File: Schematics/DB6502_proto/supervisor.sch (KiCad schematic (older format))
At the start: 32 parts, among them J9 Clock divider, SW1 Reset, U10 FT230XS, U11 74HC595, U12 74HC157, U13 ATmega644PA-PU, U14 74AC74, U15 DS1813, U16 74AC74, U17 74AC08, U8 74AC04, X1 8MHz, Y1 20MHz

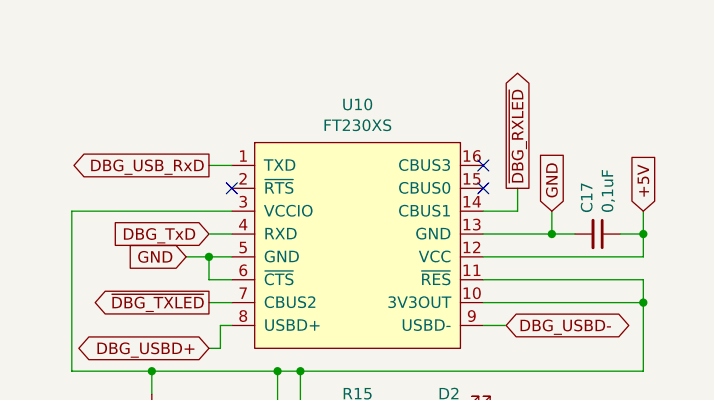
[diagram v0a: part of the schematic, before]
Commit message: Most chips placed, tracing continues
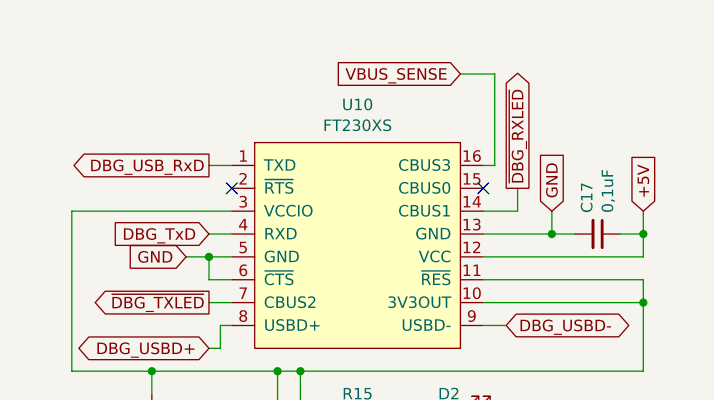
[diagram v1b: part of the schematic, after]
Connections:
- net VBUS_SENSE: now reaches U10.16 (CBUS3)
- no-connect marks 14 -> 13
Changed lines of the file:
@@
 	10300 1250 10450 1250
 NoConn ~ 10300 1150
-NoConn ~ 10300 1050
 $Comp
 L 74xx:74HC595 U11
@@
 	1    0    0    -1
 $EndComp
+Text GLabel 10200 650  0    50   Input ~ 0
+VBUS_SENSE
+Wire Wire Line
+	10300 1050 10350 1050
+Wire Wire Line
+	10350 1050 10350 650
+Wire Wire Line
+	10350 650  10200 650
 Wire Bus Line
 	3200 2200 3200 2900

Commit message: Increased capacitor footprints to 1206
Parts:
- C14, C15, C16, C17, C20, C21, C22, C23, C24, C25, C26: footprint Capacitor_SMD:C_0805_2012Metric_Pad1.15x1.40mm_HandSolder -> Capacitor_SMD:C_1206_3216Metric_Pad1.42x1.75mm_HandSolder
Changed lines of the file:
@@
 F 0 "C20" V 1350 1800 50  0000 C CNN
 F 1 "0,1uF" V 1250 1800 50  0000 C CNN
-F 2 "Capacitor_SMD:C_0805_2012Metric_Pad1.15x1.40mm_HandSolder" H 1500 1800 50  0001 C CNN
+F 2 "Capacitor_SMD:C_1206_3216Metric_Pad1.42x1.75mm_HandSolder" H 1500 1800 50  0001 C CNN
 F 3 "~" H 1500 1800 50  0001 C CNN
 	1    1500 1800
@@
 F 0 "C23" H 1342 6746 50  0000 L CNN
 F 1 "0,1uF" H 1342 6655 50  0000 L CNN
-F 2 "Capacitor_SMD:C_0805_2012Metric_Pad1.15x1.40mm_HandSolder" H 1250 6700 50  0001 C CNN
+F 2 "Capacitor_SMD:C_1206_3216Metric_Pad1.42x1.75mm_HandSolder" H 1250 6700 50  0001 C CNN
 F 3 "~" H 1250 6700 50  0001 C CNN
 	1    1250 6700
@@
 F 0 "C24" H 2292 6746 50  0000 L CNN
 F 1 "0,1uF" H 2292 6655 50  0000 L CNN
-F 2 "Capacitor_SMD:C_0805_2012Metric_Pad1.15x1.40mm_HandSolder" H 2200 6700 50  0001 C CNN
+F 2 "Capacitor_SMD:C_1206_3216Metric_Pad1.42x1.75mm_HandSolder" H 2200 6700 50  0001 C CNN
 F 3 "~" H 2200 6700 50  0001 C CNN
 	1    2200 6700
@@
 F 0 "C15" V 6921 800 50  0000 C CNN
 F 1 "0,1uF" V 7012 800 50  0000 C CNN
-F 2 "Capacitor_SMD:C_0805_2012Metric_Pad1.15x1.40mm_HandSolder" H 7150 800 50  0001 C CNN
+F 2 "Capacitor_SMD:C_1206_3216Metric_Pad1.42x1.75mm_HandSolder" H 7150 800 50  0001 C CNN
 F 3 "~" H 7150 800 50  0001 C CNN
 	1    7150 800
@@
 F 0 "C14" V 1871 800 50  0000 C CNN
 F 1 "0,1uF" V 1962 800 50  0000 C CNN
-F 2 "Capacitor_SMD:C_0805_2012Metric_Pad1.15x1.40mm_HandSolder" H 2100 800 50  0001 C CNN
+F 2 "Capacitor_SMD:C_1206_3216Metric_Pad1.42x1.75mm_HandSolder" H 2100 800 50  0001 C CNN
 F 3 "~" H 2100 800 50  0001 C CNN
 	1    2100 800
@@
 F 0 "C16" V 4721 900 50  0000 C CNN
 F 1 "0,1uF" V 4812 900 50  0000 C CNN
-F 2 "Capacitor_SMD:C_0805_2012Metric_Pad1.15x1.40mm_HandSolder" H 4950 900 50  0001 C CNN
+F 2 "Capacitor_SMD:C_1206_3216Metric_Pad1.42x1.75mm_HandSolder" H 4950 900 50  0001 C CNN
 F 3 "~" H 4950 900 50  0001 C CNN
 	1    4950 900
@@
 F 0 "C17" H 10708 1304 50  0000 R CNN
 F 1 "0,1uF" H 10708 1395 50  0000 R CNN
-F 2 "Capacitor_SMD:C_0805_2012Metric_Pad1.15x1.40mm_HandSolder" H 10800 1350 50  0001 C CNN
+F 2 "Capacitor_SMD:C_1206_3216Metric_Pad1.42x1.75mm_HandSolder" H 10800 1350 50  0001 C CNN
 F 3 "~" H 10800 1350 50  0001 C CNN
 	1    10800 1350
@@
 F 0 "C21" H 8965 2196 50  0000 L CNN
 F 1 "0,1uF" H 8965 2105 50  0000 L CNN
-F 2 "Capacitor_SMD:C_0805_2012Metric_Pad1.15x1.40mm_HandSolder" H 8888 2000 50  0001 C CNN
+F 2 "Capacitor_SMD:C_1206_3216Metric_Pad1.42x1.75mm_HandSolder" H 8888 2000 50  0001 C CNN
 F 3 "~" H 8850 2150 50  0001 C CNN
 	1    8850 2150
@@
 F 0 "C22" H 4600 4000 50  0000 R CNN
 F 1 "0,1uF" H 4600 3900 50  0000 R CNN
-F 2 "Capacitor_SMD:C_0805_2012Metric_Pad1.15x1.40mm_HandSolder" H 4700 3950 50  0001 C CNN
+F 2 "Capacitor_SMD:C_1206_3216Metric_Pad1.42x1.75mm_HandSolder" H 4700 3950 50  0001 C CNN
 F 3 "~" H 4700 3950 50  0001 C CNN
 	1    4700 3950
@@
 F 0 "C25" H 3242 6746 50  0000 L CNN
 F 1 "0,1uF" H 3242 6655 50  0000 L CNN
-F 2 "Capacitor_SMD:C_0805_2012Metric_Pad1.15x1.40mm_HandSolder" H 3150 6700 50  0001 C CNN
+F 2 "Capacitor_SMD:C_1206_3216Metric_Pad1.42x1.75mm_HandSolder" H 3150 6700 50  0001 C CNN
 F 3 "~" H 3150 6700 50  0001 C CNN
 	1    3150 6700
@@
 F 0 "C26" H 4242 6746 50  0000 L CNN
 F 1 "0,1uF" H 4242 6655 50  0000 L CNN
-F 2 "Capacitor_SMD:C_0805_2012Metric_Pad1.15x1.40mm_HandSolder" H 4150 6700 50  0001 C CNN
+F 2 "Capacitor_SMD:C_1206_3216Metric_Pad1.42x1.75mm_HandSolder" H 4150 6700 50  0001 C CNN
 F 3 "~" H 4150 6700 50  0001 C CNN
 	1    4150 6700

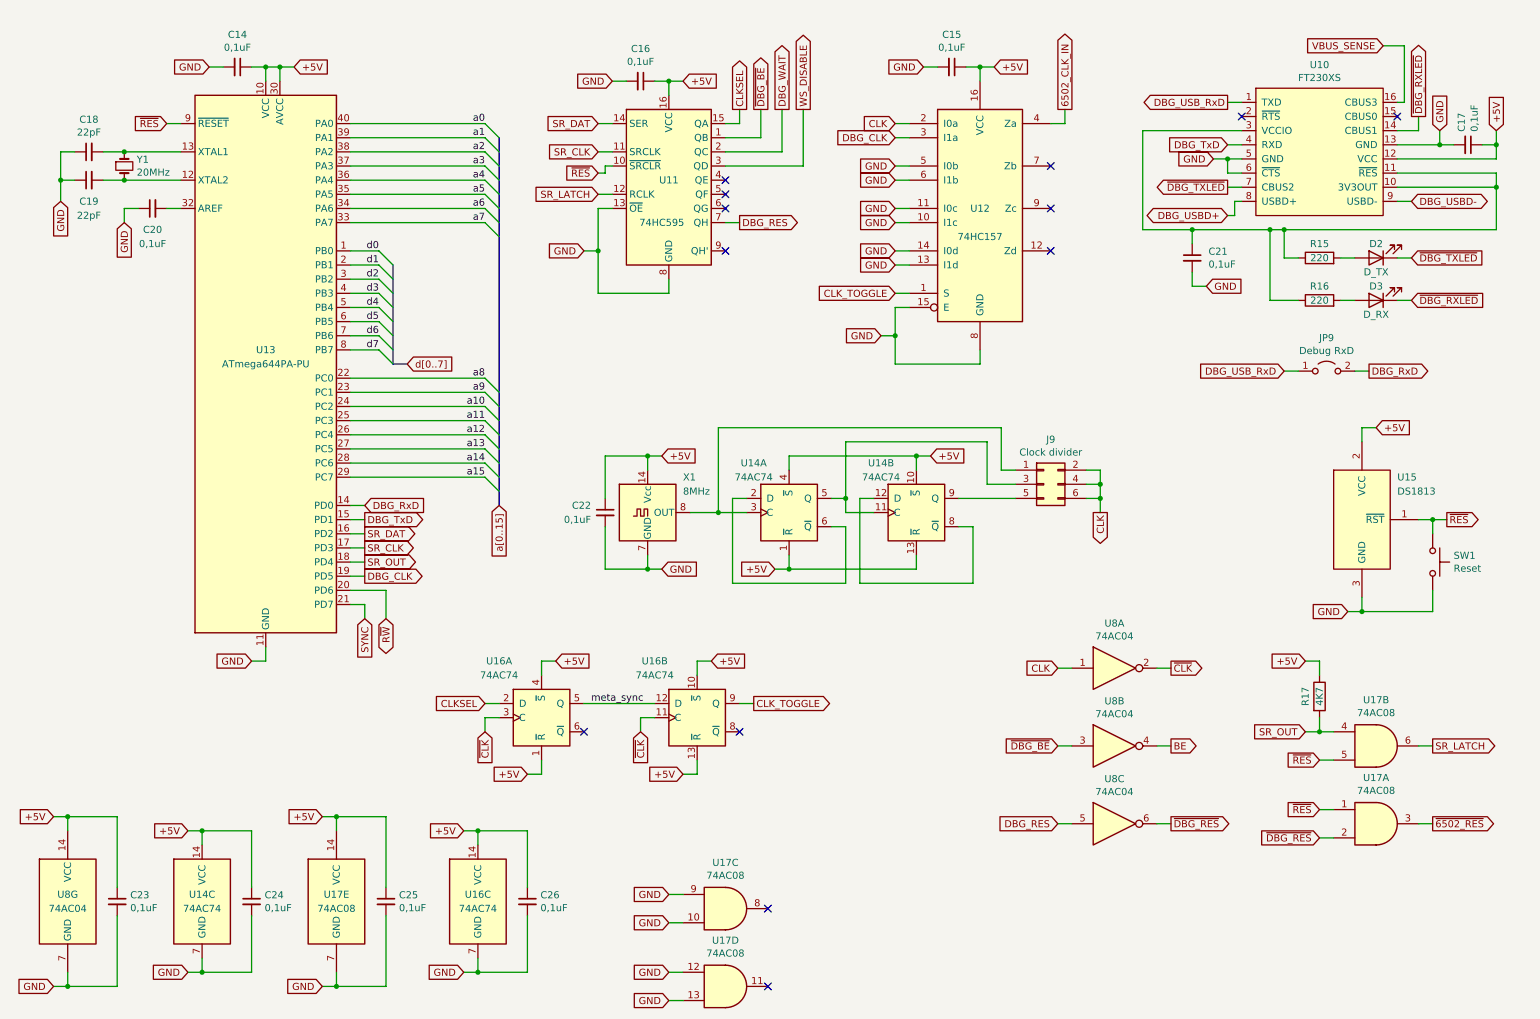
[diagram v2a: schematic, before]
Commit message: Redesigned jumpers, introduced resistor network
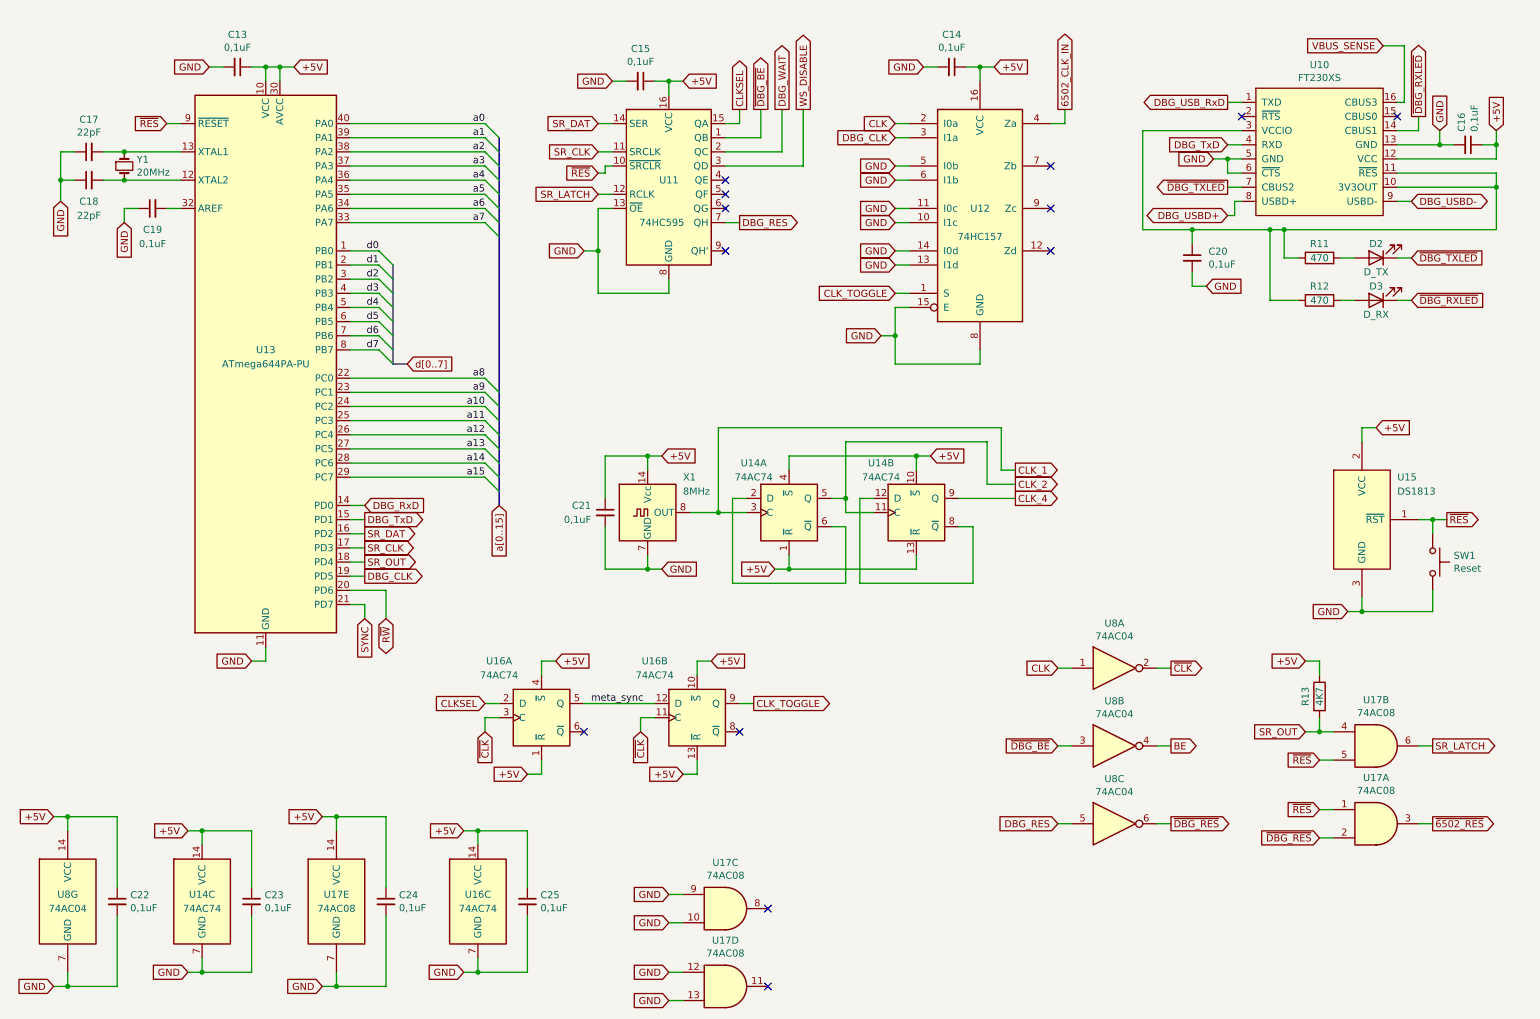
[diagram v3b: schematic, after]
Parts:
- removed J9: Clock divider, Connector_PinHeader_2.54mm:PinHeader_2x03_P2.54mm_Vertical, symbol Connector_Generic:Conn_02x03_Odd_Even
- removed JP9: Debug RxD, Connector_PinHeader_2.54mm:PinHeader_2x01_P2.54mm_Vertical, symbol Jumper:Jumper_2_Open
- R11: renamed from R15; value 220 -> 470
- R12: renamed from R16; value 220 -> 470
- renumbered C14 to C13, C15 to C14, C16 to C15, C17 to C16, C18 to C17, C19 to C18, C20 to C19, C21 to C20, C22 to C21, C23 to C22, C24 to C23, C25 to C24, C26 to C25, R17 to R13
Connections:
- net CLK_1: now reaches U14.3 (C), X1.8 (OUT)
- net CLK_2: now reaches U14.11 (C), U14.5 (Q)
- net CLK_4: now reaches U14.9 (Q)
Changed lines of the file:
@@
 $EndComp
 $Comp
-L Device:C_Small C18
+L Device:C_Small C17
 U 1 1 5F942B94
 P 1050 1400
-F 0 "C18" V 1279 1400 50  0000 C CNN
+F 0 "C17" V 1279 1400 50  0000 C CNN
 F 1 "22pF" V 1188 1400 50  0000 C CNN
 F 2 "Capacitor_THT:C_Disc_D5.0mm_W2.5mm_P2.50mm" H 1050 1400 50  0001 C CNN
@@
 $EndComp
 $Comp
-L Device:C_Small C19
+L Device:C_Small C18
 U 1 1 5F942B9A
 P 1050 1600
-F 0 "C19" V 900 1600 50  0000 C CNN
+F 0 "C18" V 900 1600 50  0000 C CNN
 F 1 "22pF" V 800 1600 50  0000 C CNN
 F 2 "Capacitor_THT:C_Disc_D5.0mm_W2.5mm_P2.50mm" H 1050 1600 50  0001 C CNN
@@
 Connection ~ 1300 1600
 $Comp
-L Device:C_Small C20
+L Device:C_Small C19
 U 1 1 5F942BA9
 P 1500 1800
-F 0 "C20" V 1350 1800 50  0000 C CNN
+F 0 "C19" V 1350 1800 50  0000 C CNN
 F 1 "0,1uF" V 1250 1800 50  0000 C CNN
 F 2 "Capacitor_SMD:C_1206_3216Metric_Pad1.42x1.75mm_HandSolder" H 1500 1800 50  0001 C CNN
@@
 	6750 2400 6850 2400
 $Comp
-L Device:C_Small C23
+L Device:C_Small C22
 U 1 1 5FAB56CF
 P 1250 6700
-F 0 "C23" H 1342 6746 50  0000 L CNN
+F 0 "C22" H 1342 6746 50  0000 L CNN
 F 1 "0,1uF" H 1342 6655 50  0000 L CNN
 F 2 "Capacitor_SMD:C_1206_3216Metric_Pad1.42x1.75mm_HandSolder" H 1250 6700 50  0001 C CNN
@@
 $EndComp
 $Comp
-L Device:C_Small C24
+L Device:C_Small C23
 U 1 1 5FAB6000
 P 2200 6700
-F 0 "C24" H 2292 6746 50  0000 L CNN
+F 0 "C23" H 2292 6746 50  0000 L CNN
 F 1 "0,1uF" H 2292 6655 50  0000 L CNN
 F 2 "Capacitor_SMD:C_1206_3216Metric_Pad1.42x1.75mm_HandSolder" H 2200 6700 50  0001 C CNN
@@
 	1850 6200 1850 6300
 $Comp
-L Device:C_Small C15
+L Device:C_Small C14
 U 1 1 5FAF8D14
 P 7150 800
-F 0 "C15" V 6921 800 50  0000 C CNN
+F 0 "C14" V 6921 800 50  0000 C CNN
 F 1 "0,1uF" V 7012 800 50  0000 C CNN
 F 2 "Capacitor_SMD:C_1206_3216Metric_Pad1.42x1.75mm_HandSolder" H 7150 800 50  0001 C CNN
@@
 	2800 7300 2700 7300
 $Comp
-L Device:C_Small C14
+L Device:C_Small C13
 U 1 1 5FB3967F
 P 2100 800
-F 0 "C14" V 1871 800 50  0000 C CNN
+F 0 "C13" V 1871 800 50  0000 C CNN
 F 1 "0,1uF" V 1962 800 50  0000 C CNN
 F 2 "Capacitor_SMD:C_1206_3216Metric_Pad1.42x1.75mm_HandSolder" H 2100 800 50  0001 C CNN
@@
 	2200 800  2300 800
 $Comp
-L Device:C_Small C16
+L Device:C_Small C15
 U 1 1 5FB5019A
 P 4950 900
-F 0 "C16" V 4721 900 50  0000 C CNN
+F 0 "C15" V 4721 900 50  0000 C CNN
 F 1 "0,1uF" V 4812 900 50  0000 C CNN
 F 2 "Capacitor_SMD:C_1206_3216Metric_Pad1.42x1.75mm_HandSolder" H 4950 900 50  0001 C CNN
@@
 	5150 900  5150 1000
 $Comp
-L Device:C_Small C17
+L Device:C_Small C16
 U 1 1 5FC939BD
 P 10800 1350
-F 0 "C17" H 10708 1304 50  0000 R CNN
+F 0 "C16" H 10708 1304 50  0000 R CNN
 F 1 "0,1uF" H 10708 1395 50  0000 R CNN
 F 2 "Capacitor_SMD:C_1206_3216Metric_Pad1.42x1.75mm_HandSolder" H 10800 1350 50  0001 C CNN
@@
 P 9750 5250
 AR Path="/5FCB90E3" Ref="R?"  Part="1"
-AR Path="/5F8F4E1E/5FCB90E3" Ref="R17"  Part="1"
-F 0 "R17" V 9650 5250 50  0000 C CNN
+AR Path="/5F8F4E1E/5FCB90E3" Ref="R13"  Part="1"
+F 0 "R13" V 9650 5250 50  0000 C CNN
 F 1 "4K7" V 9750 5250 50  0000 C CNN
 F 2 "Resistor_THT:R_Axial_DIN0207_L6.3mm_D2.5mm_P10.16mm_Horizontal" V 9680 5250 50  0001 C CNN
@@
 Wire Wire Line
 	9750 5000 9750 5100
-$Comp
-L Jumper:Jumper_2_Open JP9
-U 1 1 5FF157D7
-P 9800 2950
-F 0 "JP9" H 9800 3185 50  0000 C CNN
-F 1 "Debug RxD" H 9800 3094 50  0000 C CNN
-F 2 "Connector_PinHeader_2.54mm:PinHeader_2x01_P2.54mm_Vertical" H 9800 2950 50  0001 C CNN
-F 3 "~" H 9800 2950 50  0001 C CNN
-	1    9800 2950
-	1    0    0    -1
-$EndComp
-Text GLabel 9500 2950 0    50   Input ~ 0
-DBG_USB_RxD
-Text GLabel 10100 2950 2    50   Output ~ 0
-DBG_RxD
-Wire Wire Line
-	9500 2950 9600 2950
-Wire Wire Line
-	10000 2950 10100 2950
 Wire Wire Line
 	10450 1250 10450 1150
@@
 P 8850 2150
 AR Path="/6014B4D9/5FF0FFA6" Ref="C?"  Part="1"
-AR Path="/5F8F4E1E/5FF0FFA6" Ref="C21"  Part="1"
+AR Path="/5F8F4E1E/5FF0FFA6" Ref="C20"  Part="1"
 AR Path="/5F910E81/5FF0FFA6" Ref="C?"  Part="1"
-F 0 "C21" H 8965 2196 50  0000 L CNN
+F 0 "C20" H 8965 2196 50  0000 L CNN
 F 1 "0,1uF" H 8965 2105 50  0000 L CNN
 F 2 "Capacitor_SMD:C_1206_3216Metric_Pad1.42x1.75mm_HandSolder" H 8888 2000 50  0001 C CNN
@@
 P 9750 2150
 AR Path="/6014B4D9/5FF0FFAF" Ref="R?"  Part="1"
-AR Path="/5F8F4E1E/5FF0FFAF" Ref="R15"  Part="1"
+AR Path="/5F8F4E1E/5FF0FFAF" Ref="R11"  Part="1"
 AR Path="/5F910E81/5FF0FFAF" Ref="R?"  Part="1"
-F 0 "R15" V 9850 2150 50  0000 C CNN
-F 1 "220" V 9750 2150 50  0000 C CNN
+F 0 "R11" V 9850 2150 50  0000 C CNN
+F 1 "470" V 9750 2150 50  0000 C CNN
 F 2 "Resistor_THT:R_Axial_DIN0207_L6.3mm_D2.5mm_P10.16mm_Horizontal" V 9680 2150 50  0001 C CNN
 F 3 "~" H 9750 2150 50  0001 C CNN
@@
 P 9750 2450
 AR Path="/6014B4D9/5FF0FFC5" Ref="R?"  Part="1"
-AR Path="/5F8F4E1E/5FF0FFC5" Ref="R16"  Part="1"
+AR Path="/5F8F4E1E/5FF0FFC5" Ref="R12"  Part="1"
 AR Path="/5F910E81/5FF0FFC5" Ref="R?"  Part="1"
-F 0 "R16" V 9850 2450 50  0000 C CNN
-F 1 "220" V 9750 2450 50  0000 C CNN
+F 0 "R12" V 9850 2450 50  0000 C CNN
+F 1 "470" V 9750 2450 50  0000 C CNN
 F 2 "Resistor_THT:R_Axial_DIN0207_L6.3mm_D2.5mm_P10.16mm_Horizontal" V 9680 2450 50  0001 C CNN
 F 3 "~" H 9750 2450 50  0001 C CNN
@@
 Text GLabel 5100 4350 2    50   Input ~ 0
 GND
-Text GLabel 8200 3950 3    50   Output ~ 0
-CLK
 Wire Wire Line
 	5300 3950 5500 3950
@@
 P 4700 3950
 AR Path="/600608E6" Ref="C?"  Part="1"
-AR Path="/5F8F4E1E/600608E6" Ref="C22"  Part="1"
-F 0 "C22" H 4600 4000 50  0000 R CNN
+AR Path="/5F8F4E1E/600608E6" Ref="C21"  Part="1"
+F 0 "C21" H 4600 4000 50  0000 R CNN
 F 1 "0,1uF" H 4600 3900 50  0000 R CNN
 F 2 "Capacitor_SMD:C_1206_3216Metric_Pad1.42x1.75mm_HandSolder" H 4700 3950 50  0001 C CNN
@@
 Wire Wire Line
 	7300 4050 7200 4050
-$Comp
-L Connector_Generic:Conn_02x03_Odd_Even J9
-U 1 1 60975E70
-P 7800 3750
-F 0 "J9" H 7850 4067 50  0000 C CNN
-F 1 "Clock divider" H 7850 3976 50  0000 C CNN
-F 2 "Connector_PinHeader_2.54mm:PinHeader_2x03_P2.54mm_Vertical" H 7800 3750 50  0001 C CNN
-F 3 "~" H 7800 3750 50  0001 C CNN
-	1    7800 3750
-	1    0    0    -1
-$EndComp
 Wire Wire Line
 	7600 3750 7400 3750
@@
 	5500 3950 5700 3950
 Wire Wire Line
-	8100 3650 8200 3650
-Wire Wire Line
-	8200 3650 8200 3750
-Wire Wire Line
-	8100 3850 8200 3850
-Connection ~ 8200 3850
-Wire Wire Line
-	8200 3850 8200 3950
-Wire Wire Line
-	8100 3750 8200 3750
-Connection ~ 8200 3750
-Wire Wire Line
-	8200 3750 8200 3850
-Wire Wire Line
 	7200 3850 7600 3850
 $Comp
-L Device:C_Small C25
+L Device:C_Small C24
 U 1 1 5FB0F869
 P 3150 6700
-F 0 "C25" H 3242 6746 50  0000 L CNN
+F 0 "C24" H 3242 6746 50  0000 L CNN
 F 1 "0,1uF" H 3242 6655 50  0000 L CNN
 F 2 "Capacitor_SMD:C_1206_3216Metric_Pad1.42x1.75mm_HandSolder" H 3150 6700 50  0001 C CNN
@@
 $EndComp
 $Comp
-L Device:C_Small C26
+L Device:C_Small C25
 U 1 1 60846488
 P 4150 6700
-F 0 "C26" H 4242 6746 50  0000 L CNN
+F 0 "C25" H 4242 6746 50  0000 L CNN
 F 1 "0,1uF" H 4242 6655 50  0000 L CNN
 F 2 "Capacitor_SMD:C_1206_3216Metric_Pad1.42x1.75mm_HandSolder" H 4150 6700 50  0001 C CNN
@@
 Wire Wire Line
 	10350 650  10200 650
+Text GLabel 7600 3650 2    50   Output ~ 0
+CLK_1
+Text GLabel 7600 3750 2    50   Output ~ 0
+CLK_2
+Text GLabel 7600 3850 2    50   Output ~ 0
+CLK_4
 Wire Bus Line
 	3200 2200 3200 2900

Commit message: Working on a PCB
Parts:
- removed R13: 4K7, Resistor_THT:R_Axial_DIN0207_L6.3mm_D2.5mm_P10.16mm_Horizontal, symbol Device:R
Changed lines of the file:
@@
 NoConn ~ 5850 7300
-Wire Wire Line
-	9650 5500 9750 5500
 Wire Wire Line
 	9750 5700 9850 5700
@@
 Wire Wire Line
 	10450 5600 10550 5600
-$Comp
-L Device:R R?
-U 1 1 5FCB90E3
-P 9750 5250
-AR Path="/5FCB90E3" Ref="R?"  Part="1"
-AR Path="/5F8F4E1E/5FCB90E3" Ref="R13"  Part="1"
-F 0 "R13" V 9650 5250 50  0000 C CNN
-F 1 "4K7" V 9750 5250 50  0000 C CNN
-F 2 "Resistor_THT:R_Axial_DIN0207_L6.3mm_D2.5mm_P10.16mm_Horizontal" V 9680 5250 50  0001 C CNN
-F 3 "~" H 9750 5250 50  0001 C CNN
-	1    9750 5250
-	1    0    0    -1
-$EndComp
-Wire Wire Line
-	9750 5400 9750 5500
-Connection ~ 9750 5500
-Wire Wire Line
-	9750 5500 9850 5500
-Text GLabel 9650 5000 0    50   Input ~ 0
-+5V
-Wire Wire Line
-	9650 5000 9750 5000
-Wire Wire Line
-	9750 5000 9750 5100
 Wire Wire Line
 	10450 1250 10450 1150
@@
 Wire Bus Line
 	3950 1300 3950 3900
+Wire Wire Line
+	9650 5500 9850 5500
 $EndSCHEMATC
